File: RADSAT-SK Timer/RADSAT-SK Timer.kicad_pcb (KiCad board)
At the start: 2 copper layers, 90.2 x 95.9 mm, 116 parts, among them J101 Conn_02x26_Odd_Even, J103 Conn_02x26_Odd_Even, J201 Conn_01x07, J202 Conn_01x05, J203 Conn_01x03, J204 Conn_01x02, J205 Conn_01x02, J206 Conn_01x02, J210 ZX62WRD-B-5PC, Q101 IRLML2060, Q102 IRLML2060, Q103 IRLML2060, Q104 IRLML2060, Q105 IRLML2060, Q106 IRLML2060, Q107 IRLML2060, Q108 IRLML2060, Q109 IRLML2060, Q201 IRLML2060, Q202 IRLML2060, Q203 PJFET, Q204 PJFET, Q205 PJFET, Q206 PJFET, SW201 SW_Push, SW202 SW_Push, SW203 SW_Push, SW204 SW_Push, SW205 SW_Push, SW206 SW_Push, U101 LM397MF, U102 LM397MF, U103 LM397MF, U104 CD4052B, U202 LTC3440EMSPBF

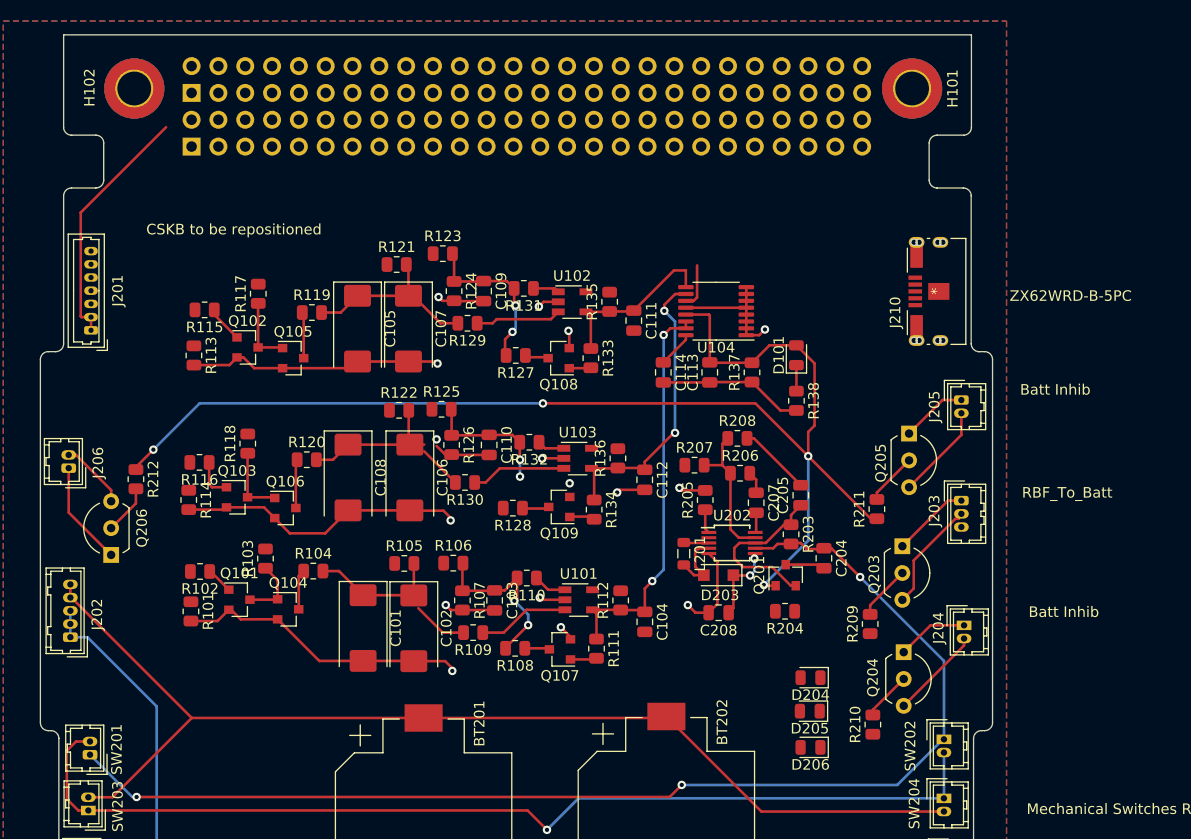
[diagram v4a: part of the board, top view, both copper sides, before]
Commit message: More components to the BOM and fixed footprints on the schematic to mathc chosen parts
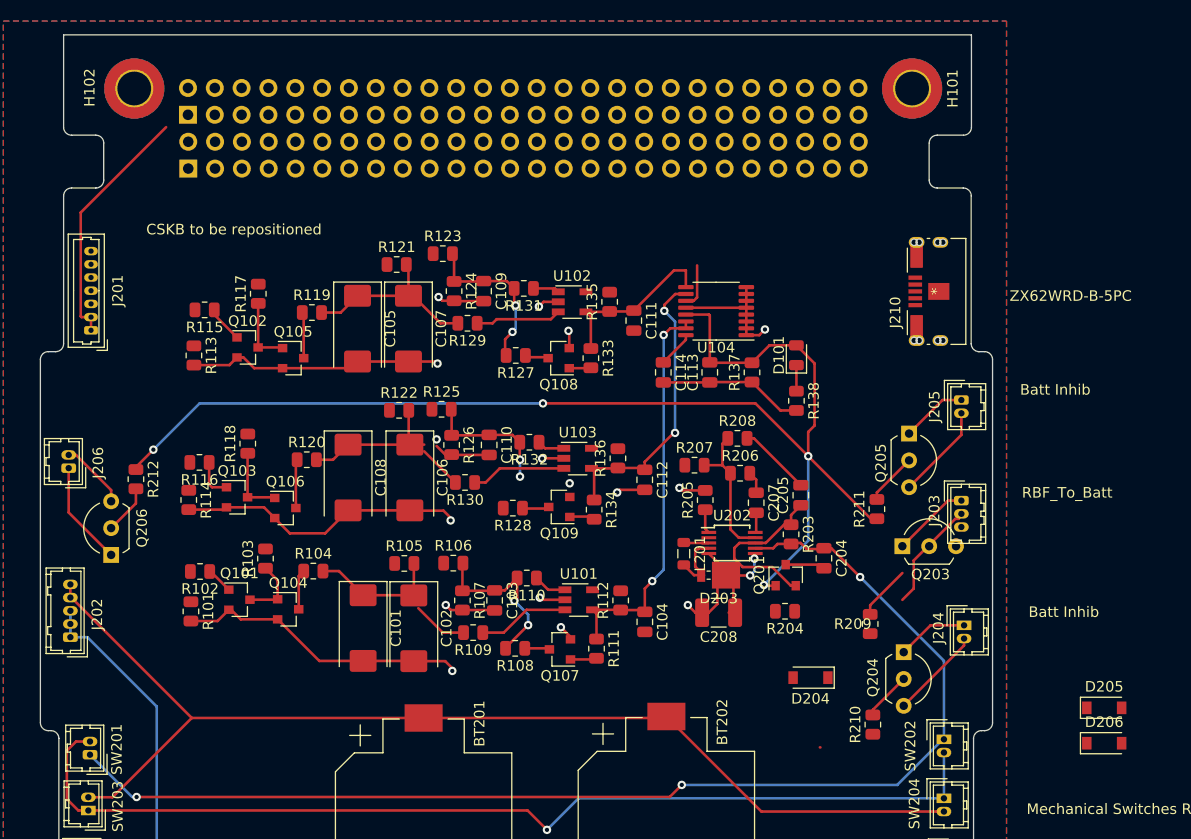
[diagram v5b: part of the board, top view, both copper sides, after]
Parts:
- C208: footprint Capacitor_SMD:C_0805_2012Metric -> Capacitor_SMD:C_1210_3225Metric_Pad1.33x2.70mm_HandSolder
- D203: value MBRM1020T3 -> MBRM120LT3G; footprint Diode_SMD:D_SOD-123F -> Diode_SMD:D_Powermite_AK
- D204, D205, D206: value D -> SM5817PL-TP; footprint Diode_SMD:D_0805_2012Metric -> Diode_SMD:D_SOD-123
- moved D205 27.9 mm to (135.6, 113.7), turned to 0 degrees
- moved D206 27.8 mm to (135.6, 117.1), turned to 0 degrees
- moved J103 2.11 mm to (48.8, 62.7)
- moved J101 2.10 mm to (48.8, 57.6)
- turned Q203 to 0 degrees
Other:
- outline, holes or cut-outs redrawn
- board text added: "For Instructional Use Only."
- board text added: "SOLIDWORKS Educational Product."

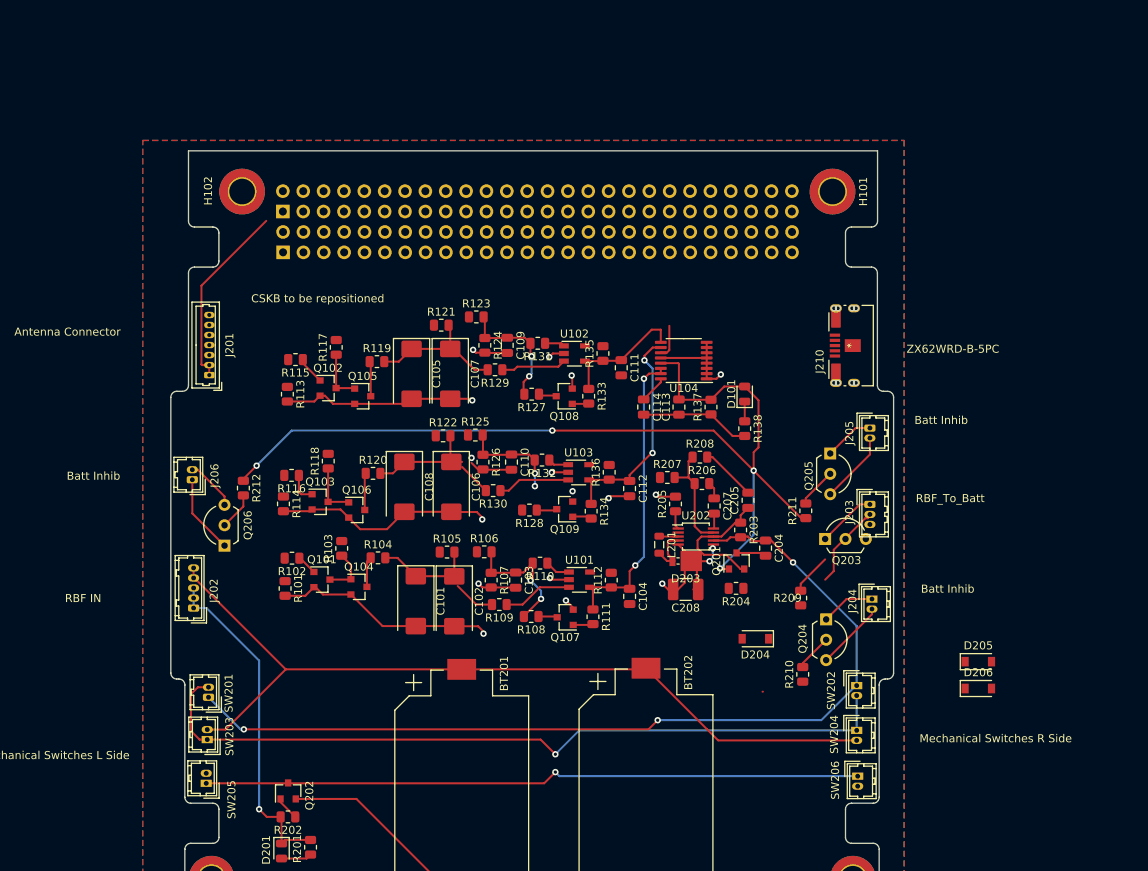
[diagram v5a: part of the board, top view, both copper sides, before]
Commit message: This commit contains more ccomponent sourcing, mainly a diode array for the inhibitor logic diodes, handsoldering footprints have been chosen for some of the sourced components, see BOM, this should help us save time and frustration in handsoldering the testboard, SW connectors were reorganized to make better connections and now both side panels must be closed to connect the battery
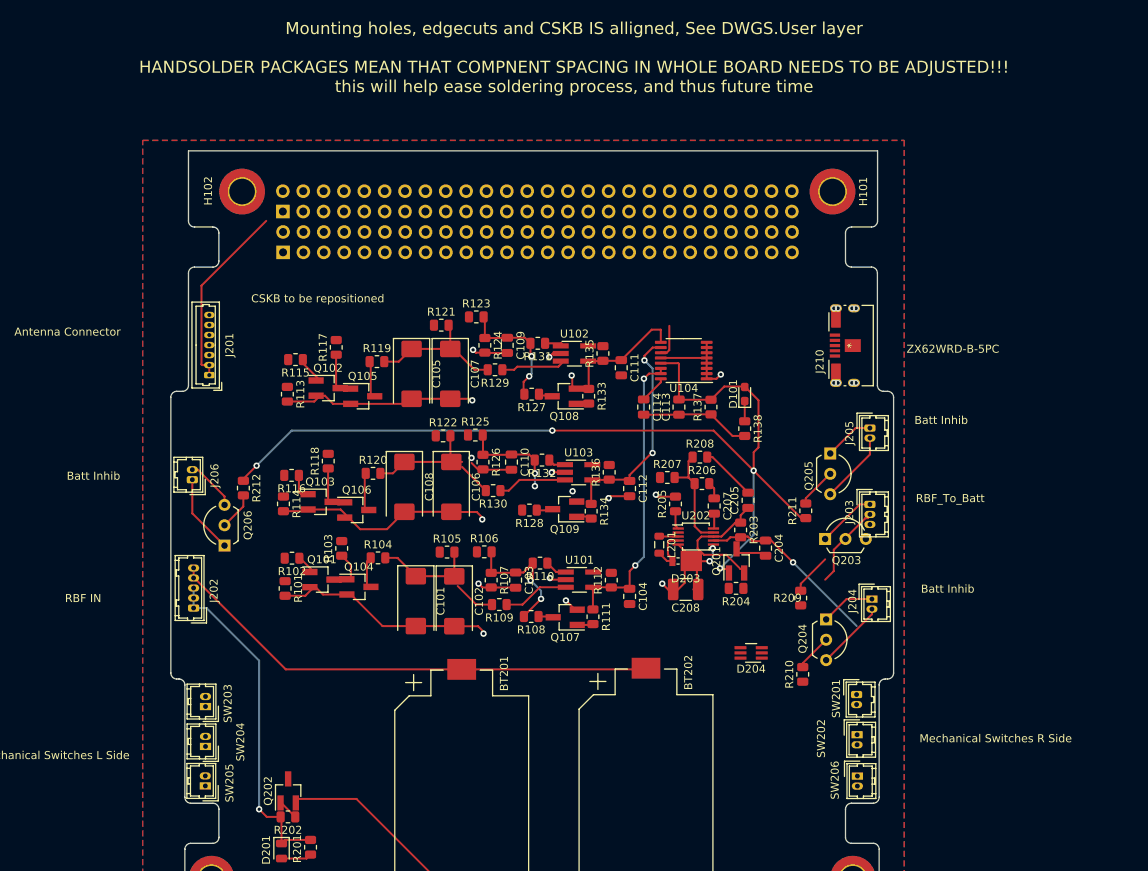
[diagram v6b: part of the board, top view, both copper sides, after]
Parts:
- removed D205, D206: SM5817PL-TP, Diode_SMD:D_SOD-123
- D101: footprint LED_SMD:LED_0805_2012Metric -> LED_SMD:LED_0603_1608Metric_Pad1.05x0.95mm_HandSolder
- D204: value SM5817PL-TP -> BAT54CDW; footprint Diode_SMD:D_SOD-123 -> Package_TO_SOT_SMD:SOT-363_SC-70-6_Handsoldering
- Q101, Q102, Q103, Q104, Q105, Q106, Q107, Q108, Q109, Q201, Q202: footprint Package_TO_SOT_SMD:SOT-23 -> Package_TO_SOT_SMD:SOT-23_Handsoldering
- U101, U102, U103: footprint Package_TO_SOT_SMD:TSOT-23-5 -> Package_TO_SOT_SMD:TSOT-23-5_HandSoldering
- moved SW204 81.3 mm to (39.2, 124.3), turned to 90 degrees
- moved SW201 80.9 mm to (120.4, 117.8), turned to 270 degrees
- moved SW202 6.13 mm to (120.4, 122.8)
- moved SW203 4.13 mm to (39.2, 119.3)
- moved D204 1.84 mm to (107.2, 112.6)
- moved SW205 0.35 mm to (39.1, 129.2)
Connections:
- D204 pad 1: Net-(D204-Pad1) -> +BATT
- D204 pad 2: +BATT -> +5V
- R209 pad 1: Net-(D204-Pad1) -> Net-(D204-Pad6)
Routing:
- net Net-(SW201-Pad2): track 97.0 -> 0.00 mm, vias 1 -> 0
- net Net-(C204-Pad1): track 114.9 -> 22.7 mm, vias 3 -> 1
- net Net-(Q202-Pad3): track 82.1 -> 0.00 mm, vias 1 -> 0
- net Net-(BT201-Pad1): track 105.5 -> 62.5 mm
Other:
- board text added: "Mounting holes, edgecuts and CSKB IS alligned, See DWGS.User layer HANDSOLDER PACKAGES MEAN THAT COMPNENT SPACING IN WHOLE BOARD NEEDS TO BE ADJUSTED!!! this will help ease soldering process, and thus future time"

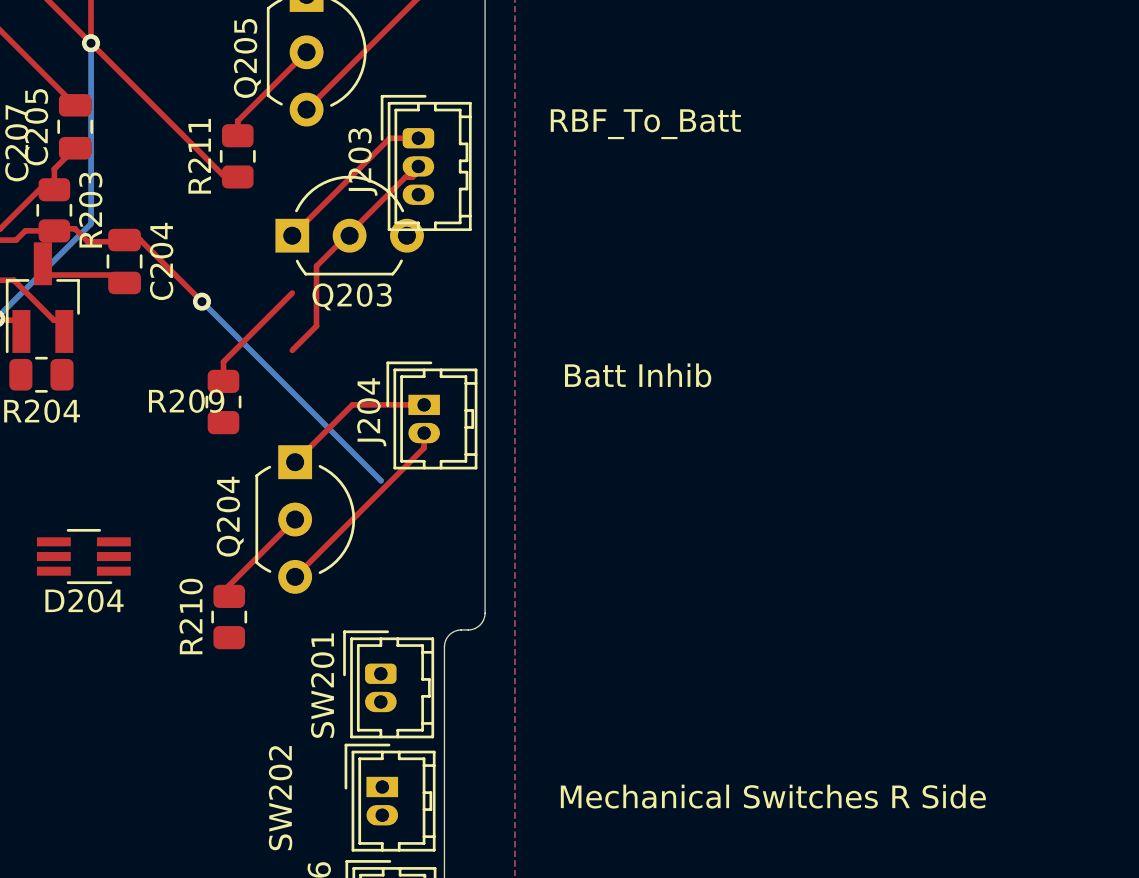
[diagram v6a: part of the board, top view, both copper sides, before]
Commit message: use of a C117 solid state relay and another mosfet for isolated connection of the pins  ie we dont care about the pin characteristic now baby
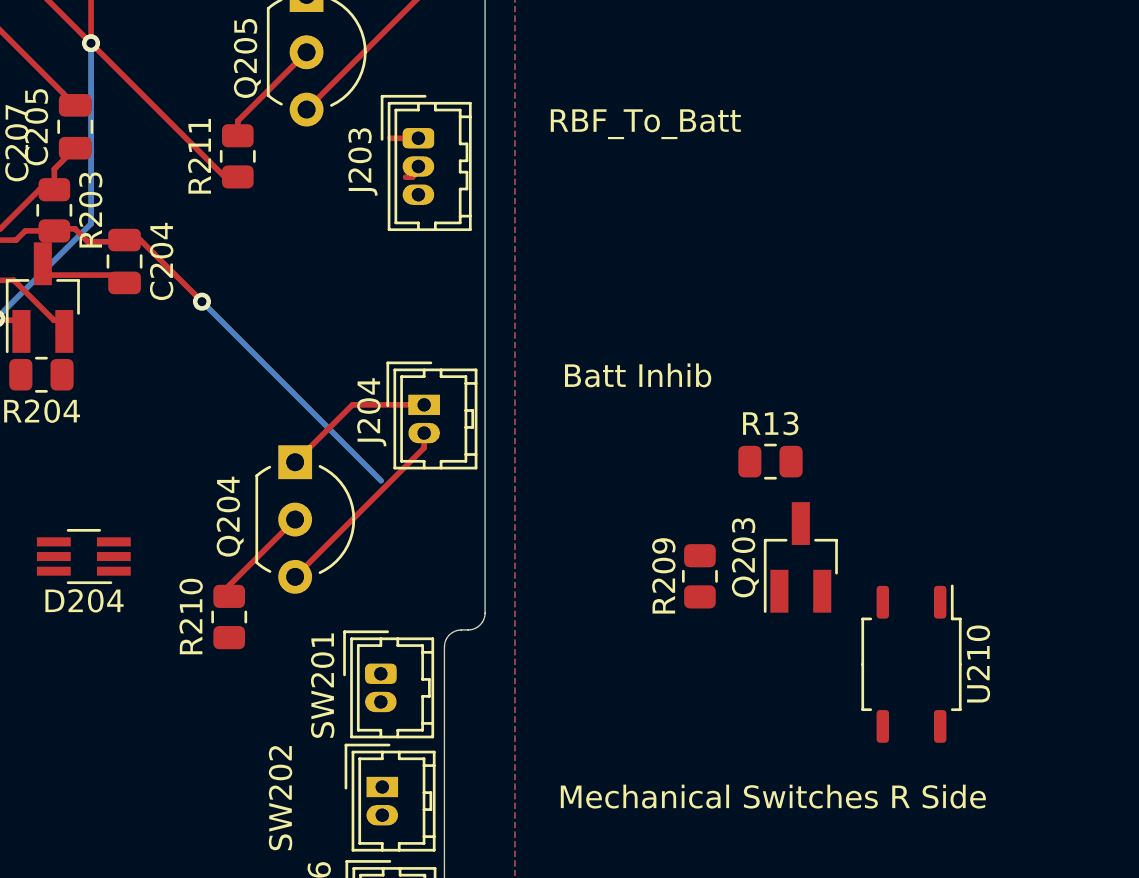
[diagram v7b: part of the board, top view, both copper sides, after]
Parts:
- added R13: 1k, Resistor_SMD:R_0805_2012Metric, F.Cu at (137.6, 108.4)
- added U210: CPC1117N, Package_SO:SOP-4_3.8x4.1mm_P2.54mm, F.Cu at (143.9, 117.4)
- Q203: value PJFET -> IRLML2060; footprint Package_TO_SOT_THT:TO-92L_Inline_Wide -> Package_TO_SOT_SMD:SOT-23_Handsoldering
- moved Q203 26.7 mm to (139.0, 112.7), turned to 90 degrees
- moved R209 22.5 mm to (134.5, 113.5), turned to 270 degrees
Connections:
- net Net-(D204-Pad6) renamed InhibV+
- Q203 pad 1: Net-(J203-Pad1) -> Net-(Q203-Pad1)
- Q203 pad 3: Net-(J203-Pad2) -> Net-(Q203-Pad3)
- R209 pad 2: Net-(Q203-Pad2) -> Net-(Q203-Pad1)
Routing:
- net Net-(J203-Pad2): track 10.6 -> 0.89 mm
- net Net-(J203-Pad1): track 7.38 -> 1.27 mm
- net Net-(Q203-Pad2): track 5.18 -> 0.00 mm
